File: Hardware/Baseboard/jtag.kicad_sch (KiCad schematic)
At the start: 43 parts, among them J3 USB_C_Receptacle_USB2.0_16P, Y1 12MHz

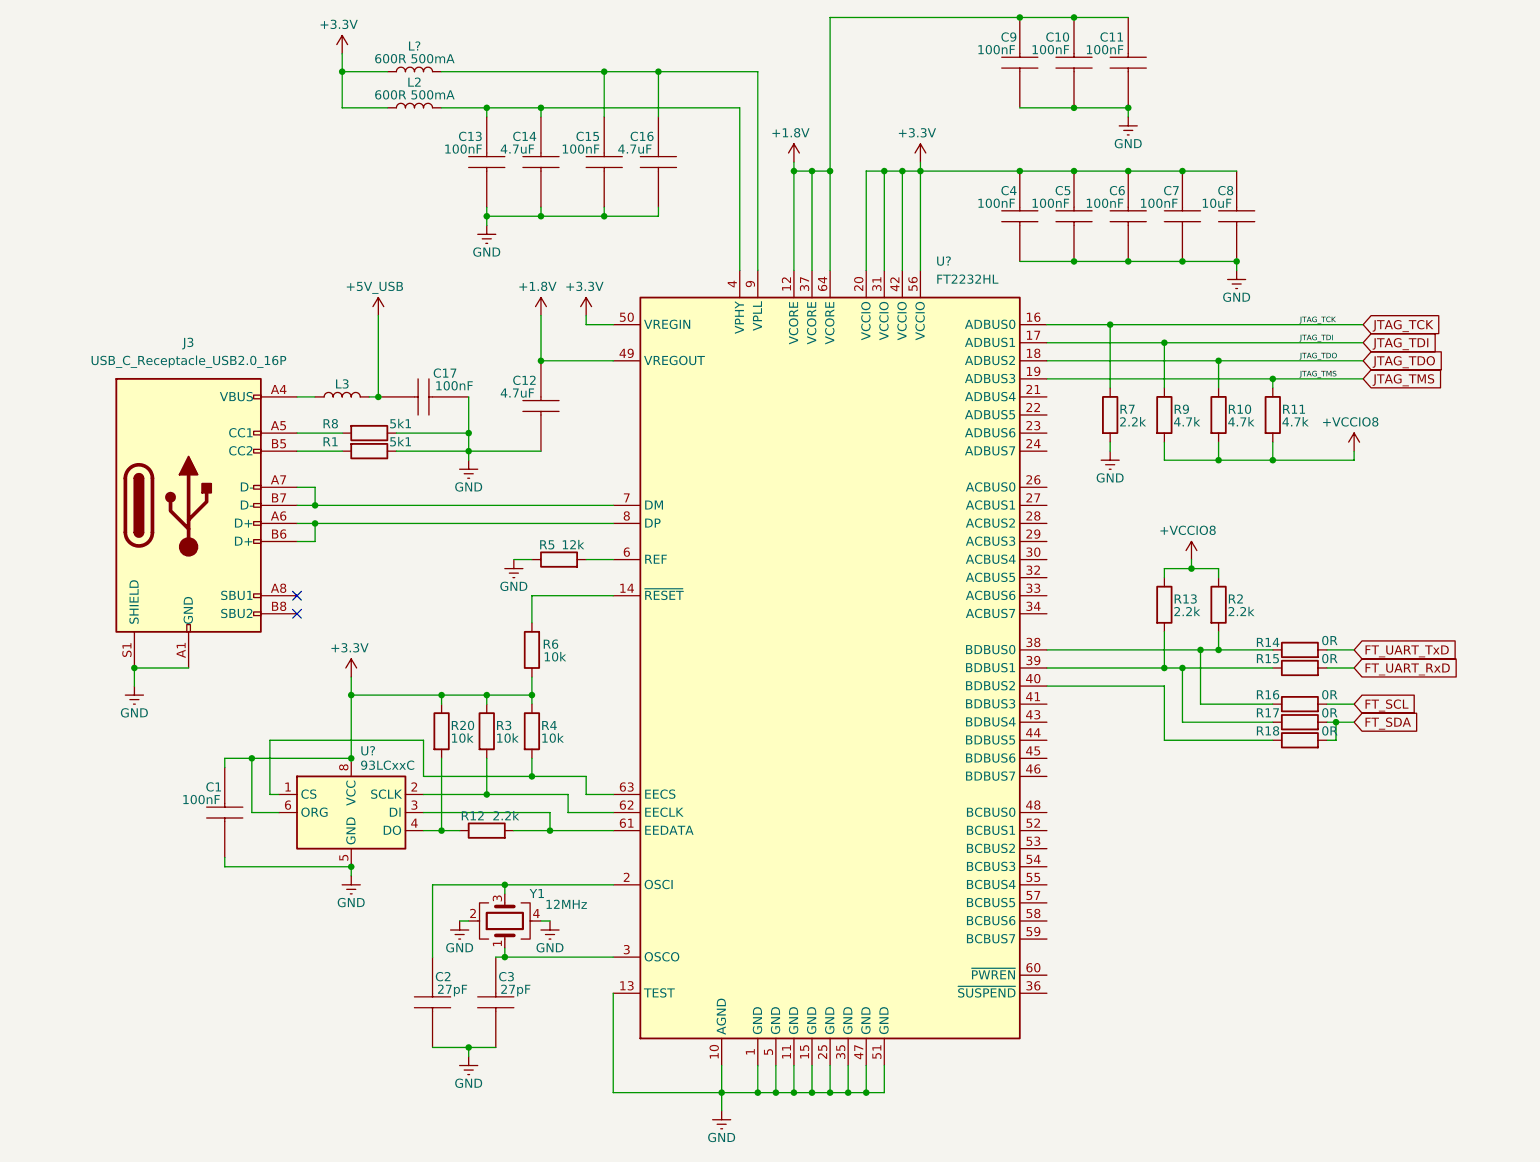
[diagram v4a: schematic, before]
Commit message: PCIe M.2 connector changed
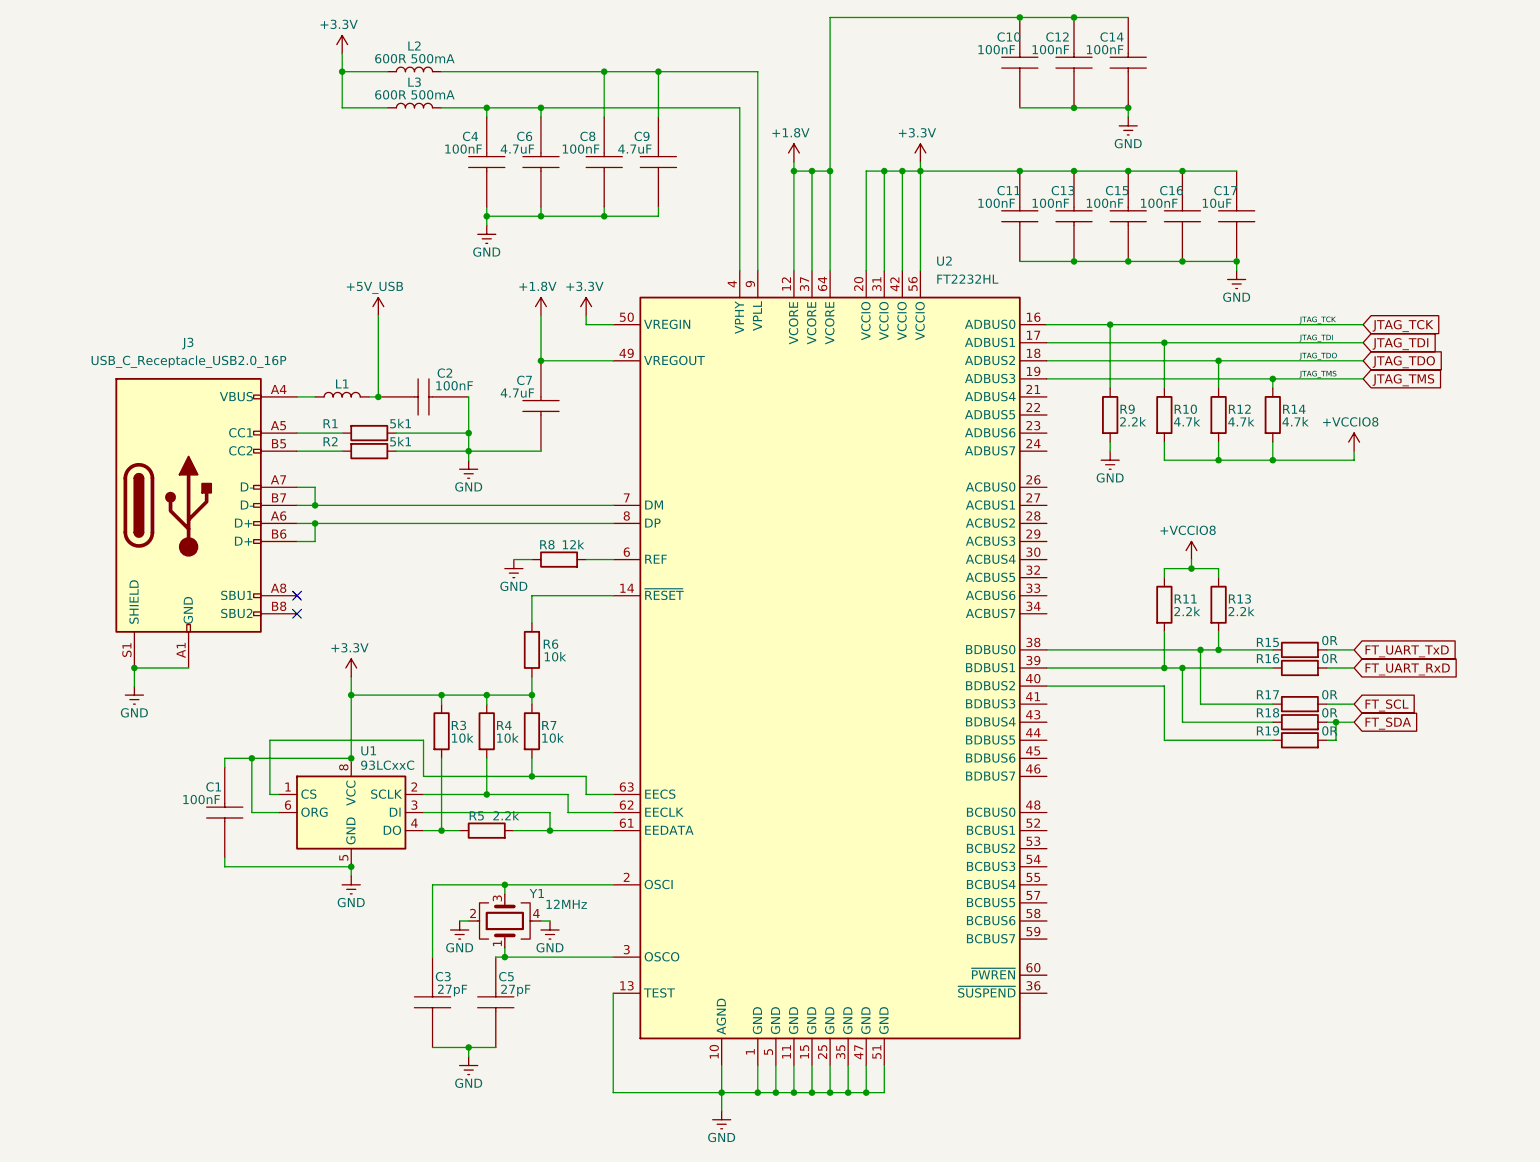
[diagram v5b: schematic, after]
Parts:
- gave numbers to parts that had none: 3
- renumbered C9 to C10, C4 to C11, C10 to C12, C5 to C13, C11 to C14, C6 to C15, C7 to C16, C8 to C17, C17 to C2, C2 to C3, C13 to C4, C3 to C5, C14 to C6, C12 to C7, C15 to C8, C16 to C9, L3 to L1, L2 to L3, R8 to R1, R9 to R10, R13 to R11, R10 to R12, R2 to R13, R11 to R14, R14 to R15, R15 to R16, R16 to R17, R17 to R18, R18 to R19, R1 to R2, R20 to R3, R3 to R4, R12 to R5, R4 to R7, R5 to R8, R7 to R9

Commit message: BB: PCIe update
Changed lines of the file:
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@@
 		(dnp no)
 		(property "Reference" "C16"
-			(at 192.786 42.164 90)
+			(at 192.278 42.164 90)
 			(effects
 				(font
@@
 		(dnp no)
 		(property "Reference" "C15"
-			(at 185.166 42.164 90)
+			(at 184.404 42.164 90)
 			(effects
 				(font
@@
 		(dnp no)
 		(property "Reference" "C13"
-			(at 177.546 42.164 90)
+			(at 176.784 42.164 90)
 			(effects
 				(font
@@
 		(dnp no)
 		(property "Reference" "C17"
-			(at 200.406 42.164 90)
+			(at 199.644 42.164 90)
 			(effects
 				(font
@@
 		(dnp no)
 		(property "Reference" "C11"
-			(at 169.926 42.164 90)
+			(at 169.418 42.164 90)
 			(effects
 				(font

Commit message: SOM: power supplies
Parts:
- R9: value 2.2k -> 4.7k; MPN 560112110087 -> 560112110245
- U2: MPN (none) -> FT2232HL-REEL; Manufacturer (none) -> FTDI
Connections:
- net +VCCIO8 is gone; now on net +3.3V: R10.2, R11.1, R12.2, R13.1, R14.2
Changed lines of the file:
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@@
 	)
 	(symbol
-		(lib_id "Device:R")
-		(at 184.15 73.66 0)
-		(unit 1)
-		(exclude_from_sim no)
-		(in_bom yes)
-		(on_board yes)
-		(dnp no)
-		(property "Reference" "R9"
-			(at 185.42 72.898 0)
-			(effects
-				(font
-					(size 1.27 1.27)
-				)
-				(justify left)
-			)
-		)
-		(property "Value" "2.2k"
-			(at 185.42 74.676 0)
-			(effects
-				(font
-					(size 1.27 1.27)
-				)
-				(justify left)
-			)
-		)
-		(property "Footprint" "Resistor_SMD:R_0402_1005Metric"
-			(at 182.372 73.66 90)
-			(effects
-				(font
-					(size 1.27 1.27)
-				)
-				(hide yes)
-			)
-		)
-		(property "Datasheet" "~"
-			(at 184.15 73.66 0)
-			(effects
-				(font
-					(size 1.27 1.27)
-				)
-				(hide yes)
-			)
-		)
-		(property "Description" "Resistor"
-			(at 184.15 73.66 0)
-			(effects
-				(font
-					(size 1.27 1.27)
-				)
-				(hide yes)
-			)
-		)
-		(property "Manufacturer" "Würth Elektronik"
-			(at 184.15 73.66 0)
-			(effects
-				(font
-					(size 1.27 1.27)
-				)
-				(hide yes)
-			)
-		)
-		(property "MPN" " 560112110087"
-			(at 184.15 73.66 0)
-			(effects
-				(font
-					(size 1.27 1.27)
-				)
-				(hide yes)
-			)
-		)
-		(pin "1"
-		)
-		(pin "2"
-		)
-		(instances
-			(project "FPGA4RISCV_BB"
-				(path "/de32abb0-ff3b-4c67-a91a-eed08140b1b2/e8a9a6a8-2e08-4606-b058-44f01919fc3b"
-					(reference "R9")
-					(unit 1)
-				)
-			)
-		)
-	)
-	(symbol
 		(lib_id "power:GNDREF")
 		(at 184.15 78.74 0)
@@
 	)
 	(symbol
-		(lib_id "power:+5V")
-		(at 195.58 93.98 0)
-		(unit 1)
-		(exclude_from_sim no)
-		(in_bom yes)
-		(on_board yes)
-		(dnp no)
-		(property "Reference" "#PWR022"
-			(at 195.58 97.79 0)
-			(effects
-				(font
-					(size 1.27 1.27)
-				)
-				(hide yes)
-			)
-		)
-		(property "Value" "+VCCIO8"
-			(at 195.072 89.916 0)
-			(effects
-				(font
-					(size 1.27 1.27)
-				)
-			)
-		)
-		(property "Footprint" ""
-			(at 195.58 93.98 0)
-			(effects
-				(font
-					(size 1.27 1.27)
-				)
-				(hide yes)
-			)
-		)
-		(property "Datasheet" ""
-			(at 195.58 93.98 0)
-			(effects
-				(font
-					(size 1.27 1.27)
-				)
-				(hide yes)
-			)
-		)
-		(property "Description" "Power symbol creates a global label with name \"+5V\""
-			(at 195.58 93.98 0)
-			(effects
-				(font
-					(size 1.27 1.27)
-				)
-				(hide yes)
-			)
-		)
-		(pin "1"
-		)
-		(instances
-			(project "FPGA4RISCV_BB"
-				(path "/de32abb0-ff3b-4c67-a91a-eed08140b1b2/e8a9a6a8-2e08-4606-b058-44f01919fc3b"
-					(reference "#PWR022")
-					(unit 1)
-				)
-			)
-		)
-	)
-	(symbol
 		(lib_id "power:GNDREF")
 		(at 92.71 144.78 0)
@@
 	(symbol
 		(lib_id "Device:R")
+		(at 184.15 73.66 0)
+		(unit 1)
+		(exclude_from_sim no)
+		(in_bom yes)
+		(on_board yes)
+		(dnp no)
+		(property "Reference" "R9"
+			(at 185.42 72.898 0)
+			(effects
+				(font
+					(size 1.27 1.27)
+				)
+				(justify left)
+			)
+		)
+		(property "Value" "4.7k"
+			(at 185.42 74.676 0)
+			(effects
+				(font
+					(size 1.27 1.27)
+				)
+				(justify left)
+			)
+		)
+		(property "Footprint" "Resistor_SMD:R_0402_1005Metric"
+			(at 182.372 73.66 90)
+			(effects
+				(font
+					(size 1.27 1.27)
+				)
+				(hide yes)
+			)
+		)
+		(property "Datasheet" "~"
+			(at 184.15 73.66 0)
+			(effects
+				(font
+					(size 1.27 1.27)
+				)
+				(hide yes)
+			)
+		)
+		(property "Description" "Resistor"
+			(at 184.15 73.66 0)
+			(effects
+				(font
+					(size 1.27 1.27)
+				)
+				(hide yes)
+			)
+		)
+		(property "Manufacturer" "Würth Elektronik"
+			(at 184.15 73.66 0)
+			(effects
+				(font
+					(size 1.27 1.27)
+				)
+				(hide yes)
+			)
+		)
+		(property "MPN" "560112110245"
+			(at 184.15 73.66 0)
+			(effects
+				(font
+					(size 1.27 1.27)
+				)
+				(hide yes)
+			)
+		)
+		(pin "1"
+		)
+		(pin "2"
+		)
+		(instances
+			(project "FPGA4RISCV_BB"
+				(path "/de32abb0-ff3b-4c67-a91a-eed08140b1b2/e8a9a6a8-2e08-4606-b058-44f01919fc3b"
+					(reference "R9")
+					(unit 1)
+				)
+			)
+		)
+	)
+	(symbol
+		(lib_id "Device:R")
 		(at 210.82 109.22 90)
 		(unit 1)
@@
 			)
 		)
+		(property "Manufacturer" "FTDI"
+			(at 144.78 109.22 0)
+			(effects
+				(font
+					(size 1.27 1.27)
+				)
+				(hide yes)
+			)
+		)
+		(property "MPN" " FT2232HL-REEL"
+			(at 144.78 109.22 0)
+			(effects
+				(font
+					(size 1.27 1.27)
+				)
+				(hide yes)
+			)
+		)
 		(pin "21"
 		)
@@
 	)
 	(symbol
-		(lib_id "power:+5V")
-		(at 218.44 78.74 0)
-		(unit 1)
-		(exclude_from_sim no)
-		(in_bom yes)
-		(on_board yes)
-		(dnp no)
-		(property "Reference" "#PWR024"
-			(at 218.44 82.55 0)
-			(effects
-				(font
-					(size 1.27 1.27)
-				)
-				(hide yes)
-			)
-		)
-		(property "Value" "+VCCIO8"
-			(at 217.932 74.676 0)
-			(effects
-				(font
-					(size 1.27 1.27)
-				)
-			)
-		)
-		(property "Footprint" ""
-			(at 218.44 78.74 0)
-			(effects
-				(font
-					(size 1.27 1.27)
-				)
-				(hide yes)
-			)
-		)
-		(property "Datasheet" ""
-			(at 218.44 78.74 0)
-			(effects
-				(font
-					(size 1.27 1.27)
-				)
-				(hide yes)
-			)
-		)
-		(property "Description" "Power symbol creates a global label with name \"+5V\""
-			(at 218.44 78.74 0)
-			(effects
-				(font
-					(size 1.27 1.27)
-				)
-				(hide yes)
-			)
-		)
-		(pin "1"
-		)
-		(instances
-			(project "FPGA4RISCV_BB"
-				(path "/de32abb0-ff3b-4c67-a91a-eed08140b1b2/e8a9a6a8-2e08-4606-b058-44f01919fc3b"
-					(reference "#PWR024")
-					(unit 1)
-				)
-			)
-		)
-	)
-	(symbol
 		(lib_id "RA8M1:885012205092")
 		(at 120.65 44.45 90)
@@
 	)
 	(symbol
+		(lib_id "power:+5V")
+		(at 218.44 78.74 0)
+		(unit 1)
+		(exclude_from_sim no)
+		(in_bom yes)
+		(on_board yes)
+		(dnp no)
+		(property "Reference" "#PWR033"
+			(at 218.44 82.55 0)
+			(effects
+				(font
+					(size 1.27 1.27)
+				)
+				(hide yes)
+			)
+		)
+		(property "Value" "+3.3V"
+			(at 217.932 74.676 0)
+			(effects
+				(font
+					(size 1.27 1.27)
+				)
+			)
+		)
+		(property "Footprint" ""
+			(at 218.44 78.74 0)
+			(effects
+				(font
+					(size 1.27 1.27)
+				)
+				(hide yes)
+			)
+		)
+		(property "Datasheet" ""
+			(at 218.44 78.74 0)
+			(effects
+				(font
+					(size 1.27 1.27)
+				)
+				(hide yes)
+			)
+		)
+		(property "Description" "Power symbol creates a global label with name \"+5V\""
+			(at 218.44 78.74 0)
+			(effects
+				(font
+					(size 1.27 1.27)
+				)
+				(hide yes)
+			)
+		)
+		(pin "1"
+		)
+		(instances
+			(project "FPGA4RISCV_BB"
+				(path "/de32abb0-ff3b-4c67-a91a-eed08140b1b2/e8a9a6a8-2e08-4606-b058-44f01919fc3b"
+					(reference "#PWR033")
+					(unit 1)
+				)
+			)
+		)
+	)
+	(symbol
 		(lib_id "Device:L")
 		(at 86.36 25.4 90)
@@
 					(unit 1)
 				)
+			)
+		)
+	)
+	(symbol
+		(lib_id "power:+5V")
+		(at 195.58 93.98 0)
+		(unit 1)
+		(exclude_from_sim no)
+		(in_bom yes)
+		(on_board yes)
+		(dnp no)
+		(property "Reference" "#PWR022"
+			(at 195.58 97.79 0)
+			(effects
+				(font
+					(size 1.27 1.27)
+				)
+				(hide yes)
+			)
+		)
+		(property "Value" "+3.3V"
+			(at 195.072 89.916 0)
+			(effects
+				(font
+					(size 1.27 1.27)
+				)
+			)
+		)
+		(property "Footprint" ""
+			(at 195.58 93.98 0)
+			(effects
+				(font
+					(size 1.27 1.27)
+				)
+				(hide yes)
+			)
+		)
+		(property "Datasheet" ""
+			(at 195.58 93.98 0)
+			(effects
+				(font
+					(size 1.27 1.27)
+				)
+				(hide yes)
+			)
+		)
+		(property "Description" "Power symbol creates a global label with name \"+5V\""
+			(at 195.58 93.98 0)
+			(effects
+				(font
+					(size 1.27 1.27)
+				)
+				(hide yes)
+			)
+		)
+		(pin "1"
+		)
+		(instances
+			(project "FPGA4RISCV_BB"
+				(path "/de32abb0-ff3b-4c67-a91a-eed08140b1b2/e8a9a6a8-2e08-4606-b058-44f01919fc3b"
+					(reference "#PWR022")
+					(unit 1)
+				)

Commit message: BB schematics: PS
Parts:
- removed C2: 100nF, Capacitor_SMD:C_0402_1005Metric, symbol RA8M1:885012205092
- removed L1: 600R 500mA, symbol Device:L
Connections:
- net +5V_USB: now also J3.A4 (VBUS), J3.A9 (VBUS), J3.B4 (VBUS), J3.B9 (VBUS)
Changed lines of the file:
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@@
 	)
 	(junction
-		(at 81.28 71.12)
-		(diameter 0)
-		(color 0 0 0 0)
-	)
-	(junction
 		(at 96.52 113.03)
 		(diameter 0)
@@
 	(wire
 		(pts
-			(xy 69.85 71.12) (xy 72.39 71.12)
+			(xy 69.85 71.12) (xy 78.74 71.12)
 		)
 		(stroke
@@
 	(wire
 		(pts
-			(xy 81.28 59.69) (xy 81.28 71.12)
+			(xy 78.74 66.04) (xy 78.74 71.12)
 		)
 		(stroke
@@
 	(wire
 		(pts
-			(xy 81.28 71.12) (xy 80.01 71.12)
-		)
-		(stroke
-			(width 0)
-			(type default)
-		)
-	)
-	(wire
-		(pts
 			(xy 144.78 165.1) (xy 144.78 168.91)
 		)
@@
 	(symbol
 		(lib_id "power:+5V")
-		(at 81.28 59.69 0)
+		(at 78.74 66.04 0)
 		(unit 1)
 		(exclude_from_sim no)
@@
 		(dnp no)
 		(property "Reference" "#PWR08"
-			(at 81.28 63.5 0)
+			(at 78.74 69.85 0)
 			(effects
 				(font
@@
 		)
 		(property "Value" "+5V_USB"
-			(at 80.772 55.626 0)
+			(at 78.232 61.976 0)
 			(effects
 				(font
@@
 		)
 		(property "Footprint" ""
-			(at 81.28 59.69 0)
+			(at 78.74 66.04 0)
 			(effects
 				(font
@@
 		)
 		(property "Datasheet" ""
-			(at 81.28 59.69 0)
+			(at 78.74 66.04 0)
 			(effects
 				(font
@@
 		)
 		(property "Description" "Power symbol creates a global label with name \"+5V\""
-			(at 81.28 59.69 0)
+			(at 78.74 66.04 0)
 			(effects
 				(font
@@
 	)
 	(symbol
-		(lib_id "RA8M1:885012205092")
-		(at 81.28 71.12 0)
-		(unit 1)
-		(exclude_from_sim no)
-		(in_bom yes)
-		(on_board yes)
-		(dnp no)
-		(property "Reference" "C2"
-			(at 90.678 67.818 0)
-			(effects
-				(font
-					(size 1.27 1.27)
-				)
-			)
-		)
-		(property "Value" "100nF"
-			(at 91.948 69.596 0)
-			(effects
-				(font
-					(size 1.27 1.27)
-				)
-			)
-		)
-		(property "Footprint" "Capacitor_SMD:C_0402_1005Metric"
-			(at 90.17 69.85 0)
-			(effects
-				(font
-					(size 1.27 1.27)
-				)
-				(justify left)
-				(hide yes)
-			)
-		)
-		(property "Datasheet" ""
-			(at 90.17 72.39 0)
-			(effects
-				(font
-					(size 1.27 1.27)
-				)
-				(justify left)
-				(hide yes)
-			)
-		)
-		(property "Description" ""
-			(at 90.17 74.93 0)
-			(effects
-				(font
-					(size 1.27 1.27)
-				)
-				(justify left)
-				(hide yes)
-			)
-		)
-		(property "Height" "0.7"
-			(at 90.17 77.47 0)
-			(effects
-				(font
-					(size 1.27 1.27)
-				)
-				(justify left)
-				(hide yes)
-			)
-		)
-		(property "Manufacturer" "Wurth Elektronik"
-			(at 90.17 85.09 0)
-			(effects
-				(font
-					(size 1.27 1.27)
-				)
-				(justify left)
-				(hide yes)
-			)
-		)
-		(property "MPN" "885012205092"
-			(at 90.17 87.63 0)
-			(effects
-				(font
-					(size 1.27 1.27)
-				)
-				(justify left)
-				(hide yes)
-			)
-		)
-		(pin "1"
-		)
-		(pin "2"
-		)
-		(instances
-			(project "FPGA4RISCV_BB"
-				(path "/de32abb0-ff3b-4c67-a91a-eed08140b1b2/e8a9a6a8-2e08-4606-b058-44f01919fc3b"
-					(reference "C2")
-					(unit 1)
-				)
-			)
-		)
-	)
-	(symbol
 		(lib_id "Device:R")
 		(at 102.87 118.11 0)
@@
 					(unit 1)
 				)
-			)
-		)
-	)
-	(symbol
-		(lib_id "Device:L")
-		(at 76.2 71.12 90)
-		(unit 1)
-		(exclude_from_sim no)
-		(in_bom yes)
-		(on_board yes)
-		(dnp no)
-		(property "Reference" "L1"
-			(at 76.2 69.342 90)
-			(effects
-				(font
-					(size 1.27 1.27)
-				)
-			)
-		)
-		(property "Value" "600R 500mA"
-			(at 76.2 69.342 90)
-			(effects
-				(font
-					(size 1.27 1.27)
-				)
-				(hide yes)
-			)
-		)
-		(property "Footprint" ""
-			(at 76.2 71.12 0)
-			(effects
-				(font
-					(size 1.27 1.27)
-				)
-				(hide yes)
-			)
-		)
-		(property "Datasheet" "~"
-			(at 76.2 71.12 0)
-			(effects
-				(font
-					(size 1.27 1.27)
-				)
-				(hide yes)
-			)
-		)
-		(property "Description" "Inductor"
-			(at 76.2 71.12 0)
-			(effects
-				(font
-					(size 1.27 1.27)
-				)
-				(hide yes)
-			)
-		)
-		(property "Manufacturer" "Wurth Elektronik"
-			(at 76.2 71.12 0)
-			(effects
-				(font
-					(size 1.27 1.27)
-				)
-				(hide yes)
-			)
-		)
-		(property "MPN" "560112110245"
-			(at 76.2 71.12 0)
-			(effects
-				(font
-					(size 1.27 1.27)
-				)
-				(hide yes)
-			)
-		)
-		(pin "2"
-		)
-		(pin "1"
-		)
-		(instances
-			(project "FPGA4RISCV_BB"
-				(path "/de32abb0-ff3b-4c67-a91a-eed08140b1b2/e8a9a6a8-2e08-4606-b058-44f01919fc3b"
-					(reference "L1")
-					(unit 1)
-				)
